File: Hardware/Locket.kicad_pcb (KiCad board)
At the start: 2 copper layers, 59 x 59 mm, 66 parts, among them Q1 LED_RGB 5050, Q2 IRLML9303, Q3 IRLML9303, SW1 SWITCH, SW2 BUTTON, SW3 DIPx4

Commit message: + Accelerometer + Proceeding with antenna & PCB
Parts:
- added C24: 0.1u, Capacitors:SMD_0603, F.Cu at (141.0, 130.8)
- added C7: 10u, Capacitors:SMD_0805, F.Cu at (135.8, 125.4)
- added C9: 0.1u, Capacitors:SMD_0603, F.Cu at (139.4, 130.8)
- added DD3: MMA8452Q, QFN:QFN16_5_3, F.Cu at (141.0, 126.0)
- added R10: 4k7, Resistors:RES_0603, F.Cu at (142.6, 130.8)
- added R11: 4k7, Resistors:RES_0603, F.Cu at (146.0, 126.6)
- F1, F2, F3, F4: footprint Resistors:SMD_0603_FUSE -> Resistors:RES_0603_FUSE; moved to B.Cu
- R1, R2, R3, R4, R5, R6, R7, R8, R9: footprint Resistors:SMD_0603 -> Resistors:RES_0603
- moved F4 48.9 mm to (115.8, 76.2), turned to 270 degrees
- moved F3 47.9 mm to (113.2, 76.2), turned to 270 degrees
- moved F2 47.6 mm to (110.6, 76.2), turned to 270 degrees
- moved F1 46.7 mm to (108.0, 76.2), turned to 270 degrees
- moved Q3 17.7 mm to (118.2, 62.8)
- moved D2 10.9 mm to (111.8, 96.4), turned to 180 degrees
- moved Q2 10.5 mm to (111.8, 93.6), turned to 90 degrees
- moved R9 0.20 mm to (116.2, 90.4)
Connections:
- DD1 pad 20: /DS1 -> (no net)
- DD1 pad 21: /DS2 -> /I2C_SCL
- DD1 pad 22: /DS3 -> /I2C_SDA
- DD1 pad 25: /DS4 -> (no net)
- DD1 pad 29: (no net) -> /DS1
- DD1 pad 32: (no net) -> /DS2
- DD1 pad 33: (no net) -> /DS3
- DD1 pad 38: (no net) -> /DS4
- DD1 pad 42: /Vibro -> /P_SCL
- DD1 pad 43: /PeriphPwr -> /P_SDA
- DD1 pad 45: /P_SCL -> /Vibro
- DD1 pad 46: /P_SDA -> /PeriphPwr
- R7 pad 2: GND -> GNDPWR

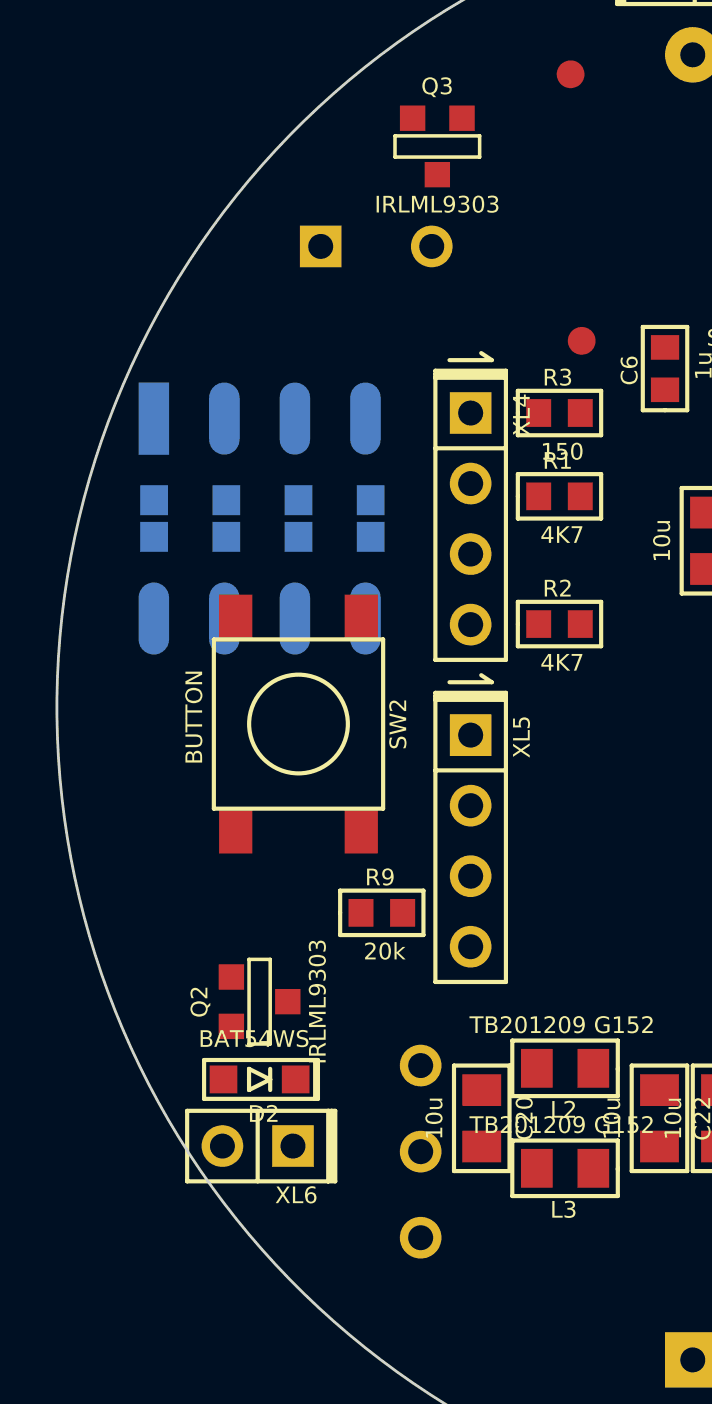
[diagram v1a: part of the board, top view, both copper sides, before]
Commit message: + Additional footprints for motor and switch
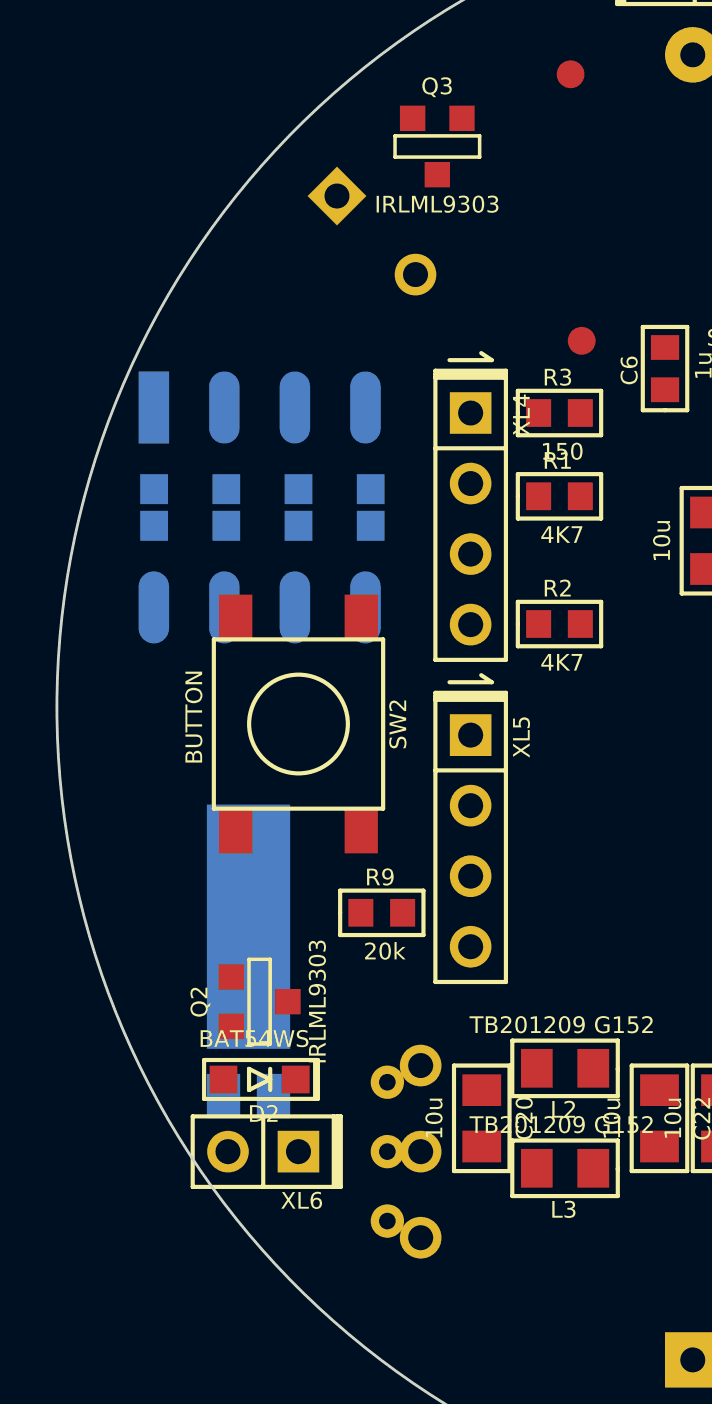
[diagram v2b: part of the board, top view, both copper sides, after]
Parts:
- added M1: MOTOR_PAD, Installations:MOTOR_KHN4NX, B.Cu at (111.4, 97.2)
- added SW4: SWITCH, Switches:SW_SS-1P2T, B.Cu at (116.4, 99.0)
- moved BZ1 0.40 mm to (116.0, 66.0), turned to 135 degrees
- moved F1 0.40 mm to (108.0, 75.8)
- moved F2 0.40 mm to (110.6, 75.8)
- moved F3 0.40 mm to (113.2, 75.8)
- moved F4 0.40 mm to (115.8, 75.8)
- moved SW3 0.40 mm to (111.8, 75.8)
- moved XL6 0.28 mm to (113.2, 99.0)
- turned SW1 to 90 degrees
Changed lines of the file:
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@@
 (kicad_pcb (version 4) (host pcbnew "(after 2015-mar-04 BZR unknown)-product")
   (general
-    (links 196)
-    (no_connects 196)
+    (links 201)
+    (no_connects 201)
     (area 104.449999 53.449999 163.550001 112.550001)
     (thickness 1.6)
@@
     (tracks 0)
     (zones 0)
-    (modules 72)
+    (modules 74)
     (nets 54)
   )
@@
   )
   (module Installations:BUZZER_HC0903 (layer B.Cu)
-    (at 116 66.4 180)
-    (fp_text reference BZ1 (at 0.0508 1.80086 180) (layer B.SilkS)
+    (at 116 66 135)
+    (fp_text reference BZ1 (at 0.0508 1.80086 135) (layer B.SilkS)
       (effects (font (size 0.59944 0.59944) (thickness 0.14986)) (justify mirror))
     )
-    (fp_text value BUZZER (at 0.09906 -2.10058 180) (layer B.SilkS)
+    (fp_text value BUZZER (at 0.09906 -2.10058 135) (layer B.SilkS)
       (effects (font (size 0.59944 0.59944) (thickness 0.14986)) (justify mirror))
     )
@@
     (fp_line (start 6.25094 -2.49936) (end 4.0005 -2.49936) (layer B.SilkS) (width 0.15))
     (fp_circle (center 0 0) (end 4.7498 0) (layer B.SilkS) (width 0.15))
-    (pad 1 thru_hole rect (at 2 0 180) (size 1.5 1.5) (drill 0.9) (layers *.Cu *.Mask B.SilkS)
+    (pad 1 thru_hole rect (at 2 0 135) (size 1.5 1.5) (drill 0.9) (layers *.Cu *.Mask B.SilkS)
       (net 6 GNDPWR))
-    (pad 2 thru_hole circle (at -2 0 180) (size 1.5 1.5) (drill 0.9) (layers *.Cu *.Mask B.SilkS)
+    (pad 2 thru_hole circle (at -2 0 135) (size 1.5 1.5) (drill 0.9) (layers *.Cu *.Mask B.SilkS)
       (net 7 /BuzzerOut))
   )
@@
   )
   (module Connectors:PLS-2 (layer F.Cu)
-    (at 113 98.8 180)
+    (at 113.2 99 180)
     (descr "Single-line connector 2-pin")
     (fp_text reference XL6 (at -0.127 -1.778 180) (layer F.SilkS)
@@
   )
   (module Switches:SW_SS-6 (layer B.Cu)
-    (at 117.6 99 270)
+    (at 117.6 99 90)
     (descr "2-position switch;11.4x5.8")
-    (fp_text reference SW1 (at 0.1 -2.3 270) (layer B.SilkS)
+    (fp_text reference SW1 (at 0.1 -2.3 90) (layer B.SilkS)
       (effects (font (size 0.6 0.6) (thickness 0.15)) (justify mirror))
     )
-    (fp_text value SWITCH (at -0.127 2.413 270) (layer B.SilkS)
+    (fp_text value SWITCH (at -0.127 2.413 90) (layer B.SilkS)
       (effects (font (size 0.6 0.6) (thickness 0.15)) (justify mirror))
     )
@@
     (fp_line (start -5.7 2.9) (end 5.7 2.9) (layer B.SilkS) (width 0.15))
     (fp_line (start 5.7 2.9) (end 5.7 -2.9) (layer B.SilkS) (width 0.15))
-    (pad 1 thru_hole circle (at -3.1 0 270) (size 1.5 1.5) (drill 0.9) (layers *.Cu *.Mask B.SilkS)
-      (net 8 +BATT))
-    (pad 2 thru_hole circle (at 0 0 270) (size 1.5 1.5) (drill 0.9) (layers *.Cu *.Mask B.SilkS)
+    (pad 1 thru_hole circle (at -3.1 0 90) (size 1.5 1.5) (drill 0.9) (layers *.Cu *.Mask B.SilkS)
+      (net 8 +BATT))
+    (pad 2 thru_hole circle (at 0 0 90) (size 1.5 1.5) (drill 0.9) (layers *.Cu *.Mask B.SilkS)
       (net 45 /BAT_IN))
-    (pad 3 thru_hole circle (at 3.1 0 270) (size 1.5 1.5) (drill 0.9) (layers *.Cu *.Mask B.SilkS))
+    (pad 3 thru_hole circle (at 3.1 0 90) (size 1.5 1.5) (drill 0.9) (layers *.Cu *.Mask B.SilkS))
   )
   (module Switches:BTN_6x6 (layer F.Cu)
@@
   )
   (module Switches:DIP_SMD_X4 (layer B.Cu)
-    (at 111.8 76.2)
+    (at 111.8 75.8)
     (descr "DIP switch 2.54x4 SMD ")
     (fp_text reference SW3 (at 5.2 2.2 90) (layer B.SilkS)
@@
   )
   (module Resistors:RES_0603_FUSE (layer B.Cu)
-    (at 108 76.2 270)
+    (at 108 75.8 270)
     (attr smd)
     (fp_text reference F1 (at -0.0635 1.27 270) (layer B.SilkS)
@@
   )
   (module Resistors:RES_0603_FUSE (layer B.Cu)
-    (at 110.6 76.2 270)
+    (at 110.6 75.8 270)
     (attr smd)
     (fp_text reference F2 (at -0.0635 1.27 270) (layer B.SilkS)
@@
   )
   (module Resistors:RES_0603_FUSE (layer B.Cu)
-    (at 113.2 76.2 270)
+    (at 113.2 75.8 270)
     (attr smd)
     (fp_text reference F3 (at -0.0635 1.27 270) (layer B.SilkS)
@@
   )
   (module Resistors:RES_0603_FUSE (layer B.Cu)
-    (at 115.8 76.2 270)
+    (at 115.8 75.8 270)
     (attr smd)
     (fp_text reference F4 (at -0.0635 1.27 270) (layer B.SilkS)
@@
     )
   )
+  (module Switches:SW_SS-1P2T (layer B.Cu)
+    (at 116.4 99 90)
+    (fp_text reference SW4 (at 0 -1.3 90) (layer B.SilkS)
+      (effects (font (size 0.6 0.6) (thickness 0.15)) (justify mirror))
+    )
+    (fp_text value SWITCH (at -0.2 1.2 90) (layer B.Fab)
+      (effects (font (size 0.6 0.6) (thickness 0.15)) (justify mirror))
+    )
+    (fp_line (start 4.3 1.8) (end 4.3 -1.8) (layer B.SilkS) (width 0.15))
+    (fp_line (start 4.3 -1.8) (end -4.3 -1.8) (layer B.SilkS) (width 0.15))
+    (fp_line (start -4.3 -1.8) (end -4.3 1.8) (layer B.SilkS) (width 0.15))
+    (fp_line (start -4.3 1.8) (end 4.3 1.8) (layer B.SilkS) (width 0.15))
+    (pad 1 thru_hole circle (at -2.5 0 90) (size 1.2 1.2) (drill 0.6) (layers *.Cu *.Mask B.SilkS)
+      (net 8 +BATT))
+    (pad 2 thru_hole circle (at 0 0 90) (size 1.2 1.2) (drill 0.6) (layers *.Cu *.Mask B.SilkS)
+      (net 45 /BAT_IN))
+    (pad 3 thru_hole circle (at 2.5 0 90) (size 1.2 1.2) (drill 0.6) (layers *.Cu *.Mask B.SilkS))
+  )
+  (module Installations:MOTOR_KHN4NX (layer B.Cu)
+    (at 111.4 97.2 270)
+    (fp_text reference M1 (at -3.7 2.8 270) (layer B.SilkS)
+      (effects (font (size 0.6 0.6) (thickness 0.15)) (justify mirror))
+    )
+    (fp_text value MOTOR_PAD (at -9.6 2.8 270) (layer B.SilkS)
+      (effects (font (size 0.6 0.6) (thickness 0.15)) (justify mirror))
+    )
+    (fp_line (start -10.8 -2.3) (end -15.5 -2.3) (layer B.SilkS) (width 0.2))
+    (fp_line (start -15.5 -2.3) (end -15.5 2.3) (layer B.SilkS) (width 0.2))
+    (fp_line (start -15.5 2.3) (end -10.8 2.3) (layer B.SilkS) (width 0.2))
+    (fp_line (start 0 0) (end 0 -2.3) (layer B.SilkS) (width 0.2))
+    (fp_line (start 0 -2.3) (end -10.8 -2.3) (layer B.SilkS) (width 0.2))
+    (fp_line (start -10.8 -2.3) (end -10.8 2.3) (layer B.SilkS) (width 0.2))
+    (fp_line (start -10.8 2.3) (end 0 2.3) (layer B.SilkS) (width 0.2))
+    (fp_line (start 0 2.3) (end 0 0) (layer B.SilkS) (width 0.2))
+    (pad 1 smd rect (at -0.2 0.9 270) (size 1.6 1.2) (layers B.Cu B.Mask)
+      (net 6 GNDPWR))
+    (pad 2 smd rect (at -0.2 -0.9 270) (size 1.6 1.2) (layers B.Cu B.Mask)
+      (net 15 /VibroOut))
+    (pad PAD smd rect (at -6.3 0 270) (size 8.8 3) (layers B.Cu B.Mask)
+      (net 6 GNDPWR))
+  )
   (gr_circle (center 111.2 87.6) (end 117.2 87.6) (layer B.SilkS) (width 0.2))

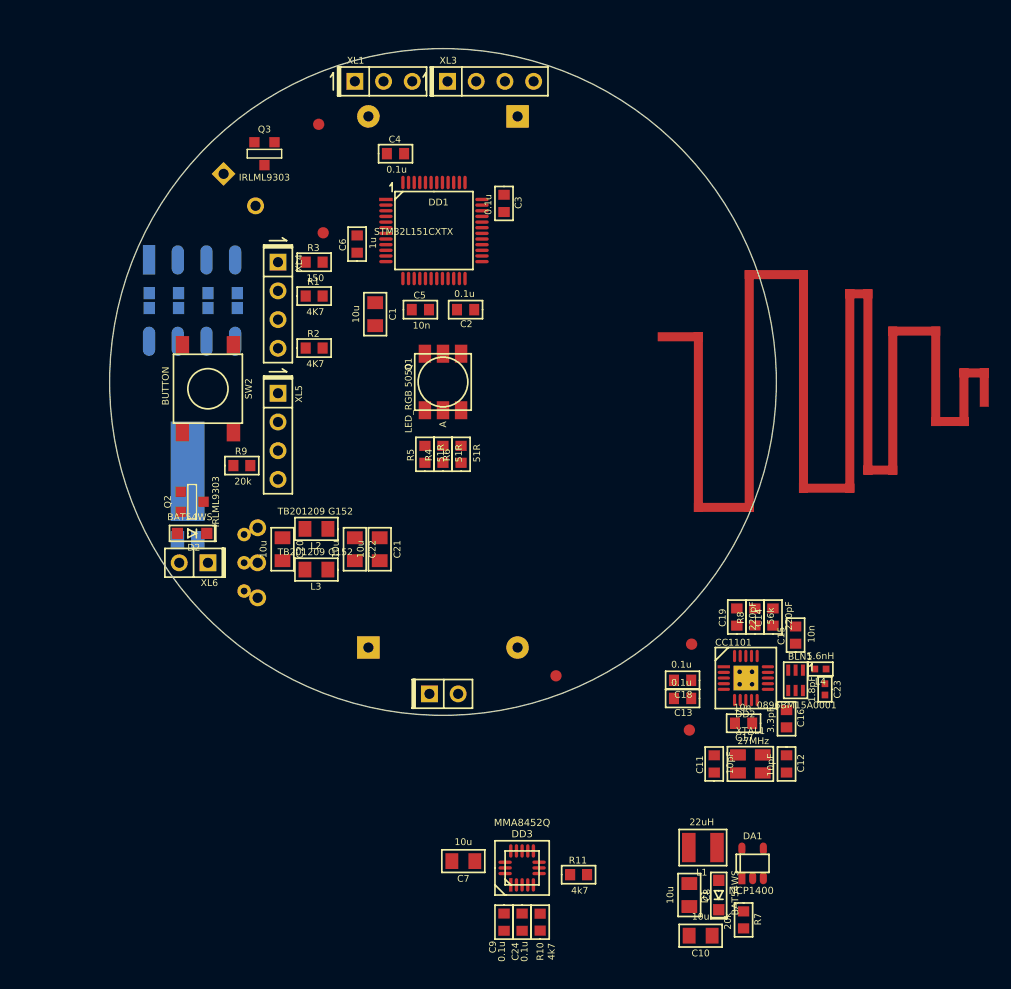
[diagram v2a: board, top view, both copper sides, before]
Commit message: + PCB routed, but DRC not tested
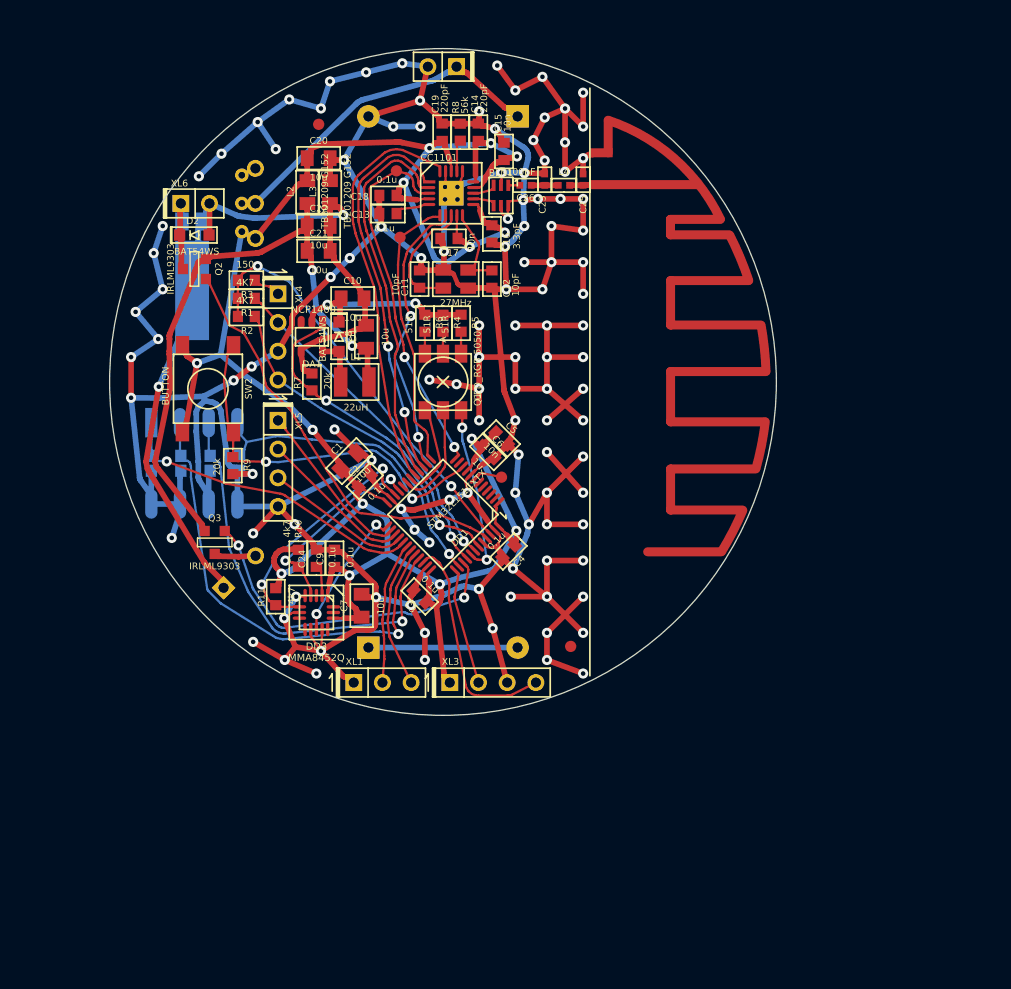
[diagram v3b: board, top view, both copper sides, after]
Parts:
- added C25: TBD, Capacitors:CAP_0402, F.Cu at (146.4, 65.1)
- added C26: 100pF, Capacitors:CAP_0402, F.Cu at (141.3, 65.6)
- ANT1: value ANT_PCB_MONO -> ANT_PCB_MONO_2PIN; footprint Radio:ANT_868_SEIDHE -> Radio:ANT_868_ROUND_F
- C1, C10, C20, C21, C22, C7, C8: footprint Capacitors:SMD_0805 -> Capacitors:CAP_0805
- C11, C12, C13, C14, C15, C16, C17, C18, C19, C2, C24, C3, C4, C5, C6, C9: footprint Capacitors:SMD_0603 -> Capacitors:CAP_0603
- C23: value 1.8pF -> TBD; footprint Capacitors:SMD_0402 -> Capacitors:CAP_0402
- L1: footprint Inductors:SMD_1210_LQH32C -> Inductors:IND_1210_LQH32C
- L2, L3: footprint Inductors:SMD_0805 -> Inductors:IND_0805
- L4: value 5.6nH -> TBD; footprint Inductors:SMD_0402 -> Inductors:IND_0402
- moved C10 64.3 mm to (126.0, 75.6), turned to 0 degrees
- moved R7 61.0 mm to (122.4, 83.0), turned to 90 degrees
- moved DA1 60.8 mm to (122.4, 79.0), turned to 180 degrees
- moved D1 59.7 mm to (124.8, 79.0), turned to 270 degrees
- moved C8 57.1 mm to (127.2, 79.0), turned to 90 degrees
- moved XL2 55.6 mm to (135.2, 55.1), turned to 180 degrees
- moved XL3 53.2 mm to (134.6, 109.6)
- moved XL1 53.2 mm to (126.1, 109.6)
- moved C23 51.5 mm to (143.0, 65.1), turned to 90 degrees
- moved L1 51.4 mm to (126.2, 83.0), turned to 0 degrees
- moved TP2 50.6 mm to (130.2, 70.2)
- moved BLN1 50.2 mm to (139.1, 66.5)
- moved C13 50.2 mm to (129.1, 68.1)
- moved C14 50.2 mm to (137.1, 60.9)
- moved C17 50.2 mm to (134.5, 70.3)
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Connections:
- ANT1 pad 1: /ANT -> /ANT2
- C23 pad 1: /ANT -> /ANT1
- DD1 pad 25: (no net) -> /ACC_INT1
- DD3 pad 11: (no net) -> /ACC_INT1
- L4 pad 1: /ANT -> /ANT2
- L4 pad 2: /RF3 -> /ANT1
- XL3 pad 1: +3.3V -> +BATT
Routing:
- net GND: track 0.00 -> 531.9 mm, vias 0 -> 118
- net +BATT: track 0.00 -> 208.3 mm, vias 0 -> 14
- net GNDPWR: track 0.00 -> 74.4 mm, vias 0 -> 2
- net /PWR_F: track 0.00 -> 54.8 mm, vias 0 -> 2
- net /DS2: track 0.00 -> 41.3 mm, vias 0 -> 1
- net /DS3: track 0.00 -> 37.4 mm, vias 0 -> 1
- net /PeriphPwr: track 0.00 -> 37.2 mm, vias 0 -> 2
- net /Vibro: track 0.00 -> 37.1 mm
- net /CC_MOSI: track 0.00 -> 36.3 mm
- net /CC_SCK: track 0.00 -> 34.3 mm, vias 0 -> 2
- net /CC_MISO: track 0.00 -> 34.0 mm
- net Net-(DD1-Pad10): track 0.00 -> 33.9 mm, vias 0 -> 2
- net /CC_GDO2: track 0.00 -> 32.5 mm, vias 0 -> 2
- net /BAT_IN: track 0.00 -> 30.5 mm
- net /P_SDA: track 0.00 -> 30.1 mm, vias 0 -> 1
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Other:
- net class Default: trace_width 0.25 -> 0.2; via_dia 0.6 -> 0.9
- net class Wide added: clearance 0.2, trace_width 0.5, via_dia 0.9, via_drill 0.4

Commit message: * PCB sent to production
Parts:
- moved RP1 5.83 mm to (117.2, 60.8)
- moved C17 0.41 mm to (134.8, 70.6)
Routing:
- net GND: track 531.9 -> 538.3 mm, vias 118 -> 119
- net /I2C_SCL: track 17.3 -> 17.9 mm
- net +BATT: track 208.3 -> 208.9 mm
- added copper zone on B.Cu, net GND
- added copper zone on F.Cu, net GND
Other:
- rule pad_to_mask_clearance: 0 -> 0.1
- board text added: "Accelerometer"
- board text added: "Button"
- board text added: "Just Pins"
- board text added: "LED"
- board text added: "LED Pwr"
- board text added: "Motor"
- board text added: "Pill"
- board text added: "Power Filter"
- board text added: "Radio"
- board text added: "SWD"
- board text added: "Sound"
- board text added: "UART"
